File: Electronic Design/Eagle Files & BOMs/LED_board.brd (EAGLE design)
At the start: 49.2 x 29.2 mm, 12 parts

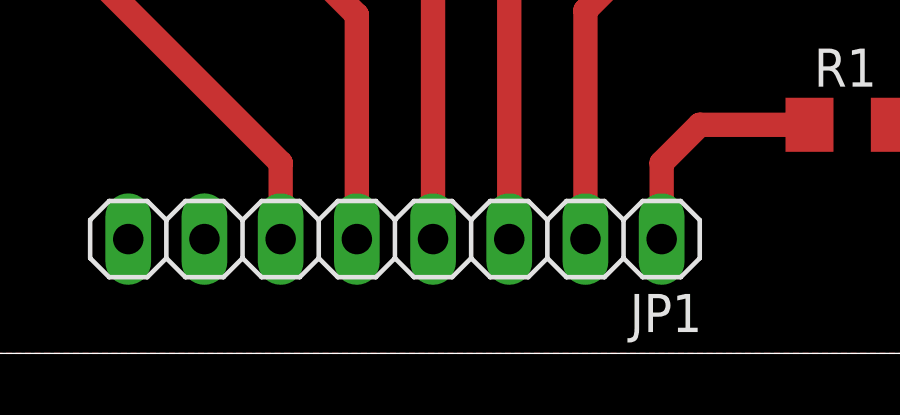
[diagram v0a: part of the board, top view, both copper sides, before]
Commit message: changed that name of header to LED_CONTROL_IN / OUT
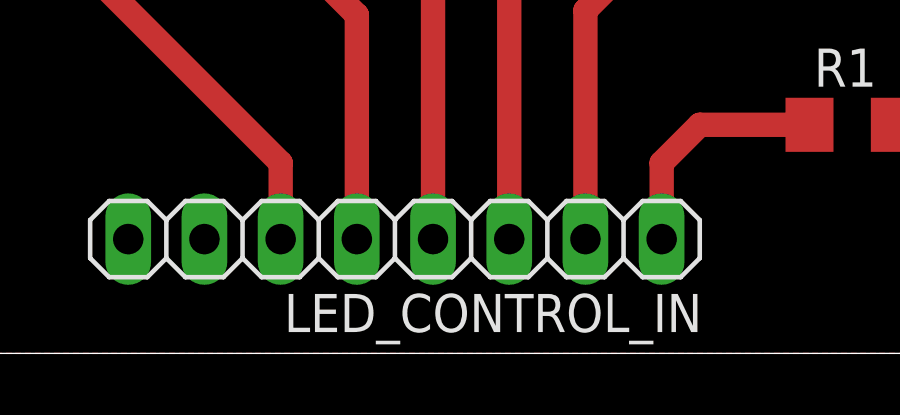
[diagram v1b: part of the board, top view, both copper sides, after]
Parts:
- renumbered JP1 to LED_CONTROL_IN
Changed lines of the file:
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@@
 </autorouter>
 <elements>
-<element name="JP1" library="pinhead" package="1X08" value="" x="19.05" y="3.81" rot="R180"/>
+<element name="LED_CONTROL_IN" library="pinhead" package="1X08" value="" x="19.05" y="3.81" rot="R180"/>
 <element name="LED1" library="led" package="LED5MM" value="" x="41.91" y="7.62" smashed="yes">
 <attribute name="NAME" x="46.4566" y="5.715" size="1.27" layer="25" ratio="10" rot="R90"/>
@@
 <signals>
 <signal name="+5V">
-<contactref element="JP1" pad="7"/>
+<contactref element="LED_CONTROL_IN" pad="7"/>
 </signal>
 <signal name="N$1">
-<contactref element="JP1" pad="1"/>
+<contactref element="LED_CONTROL_IN" pad="1"/>
 <contactref element="R1" pad="1"/>
 <wire x1="27.94" y1="3.81" x2="27.94" y2="6.35" width="0.8128" layer="1"/>
@@
 </signal>
 <signal name="N$2">
-<contactref element="JP1" pad="2"/>
+<contactref element="LED_CONTROL_IN" pad="2"/>
 <contactref element="R2" pad="1"/>
 <wire x1="25.4" y1="3.81" x2="25.4" y2="11.43" width="0.8128" layer="1"/>
@@
 <signal name="N$3">
 <contactref element="R3" pad="1"/>
-<contactref element="JP1" pad="3"/>
+<contactref element="LED_CONTROL_IN" pad="3"/>
 <wire x1="22.86" y1="3.81" x2="22.86" y2="13.97" width="0.8128" layer="1"/>
 <wire x1="22.86" y1="13.97" x2="31.75" y2="22.86" width="0.8128" layer="1"/>
@@
 </signal>
 <signal name="N$5">
-<contactref element="JP1" pad="6"/>
+<contactref element="LED_CONTROL_IN" pad="6"/>
 <contactref element="LED6" pad="A"/>
 <wire x1="15.24" y1="3.81" x2="15.24" y2="6.35" width="0.8128" layer="1"/>
@@
 <signal name="N$6">
 <contactref element="R5" pad="1"/>
-<contactref element="JP1" pad="5"/>
+<contactref element="LED_CONTROL_IN" pad="5"/>
 <wire x1="17.78" y1="3.81" x2="17.78" y2="11.278" width="0.8128" layer="1"/>
 <wire x1="17.78" y1="11.278" x2="15.24" y2="13.818" width="0.8128" layer="1"/>
@@
 <signal name="N$4">
 <contactref element="R4" pad="1"/>
-<contactref element="JP1" pad="4"/>
+<contactref element="LED_CONTROL_IN" pad="4"/>
 <wire x1="20.32" y1="3.81" x2="20.32" y2="13.818" width="0.8128" layer="1"/>
 </signal>
 <signal name="GND">
-<contactref element="JP1" pad="8"/>
+<contactref element="LED_CONTROL_IN" pad="8"/>
 <contactref element="LED1" pad="K"/>
 <contactref element="LED2" pad="K"/>
